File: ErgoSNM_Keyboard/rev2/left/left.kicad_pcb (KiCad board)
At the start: 2 copper layers, 115.6 x 106.7 mm, 111 parts, among them J1 USB_C_Receptacle_USB2.0, J2 USB_C_Receptacle_USB2.0, J3 PJ-393_TRRS_8P, J4 Conn_01x08, SW1 BOOT, SW2 RESET, U1 RT9013-33GB, U2 SRV05-4, U3 W25Q128JVS, U4 RP2040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

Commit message: Update silk and logo
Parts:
- moved kibuzzard-63A148C1 119.2 mm to (73.6, 116.4)
- moved G*** 112.2 mm to (90.3, 114.3)

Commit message: Update logo
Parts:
- moved G*** 20.4 mm to (82.5, 95.4)
- moved kibuzzard-63A148C1 19.2 mm to (74.1, 97.2)

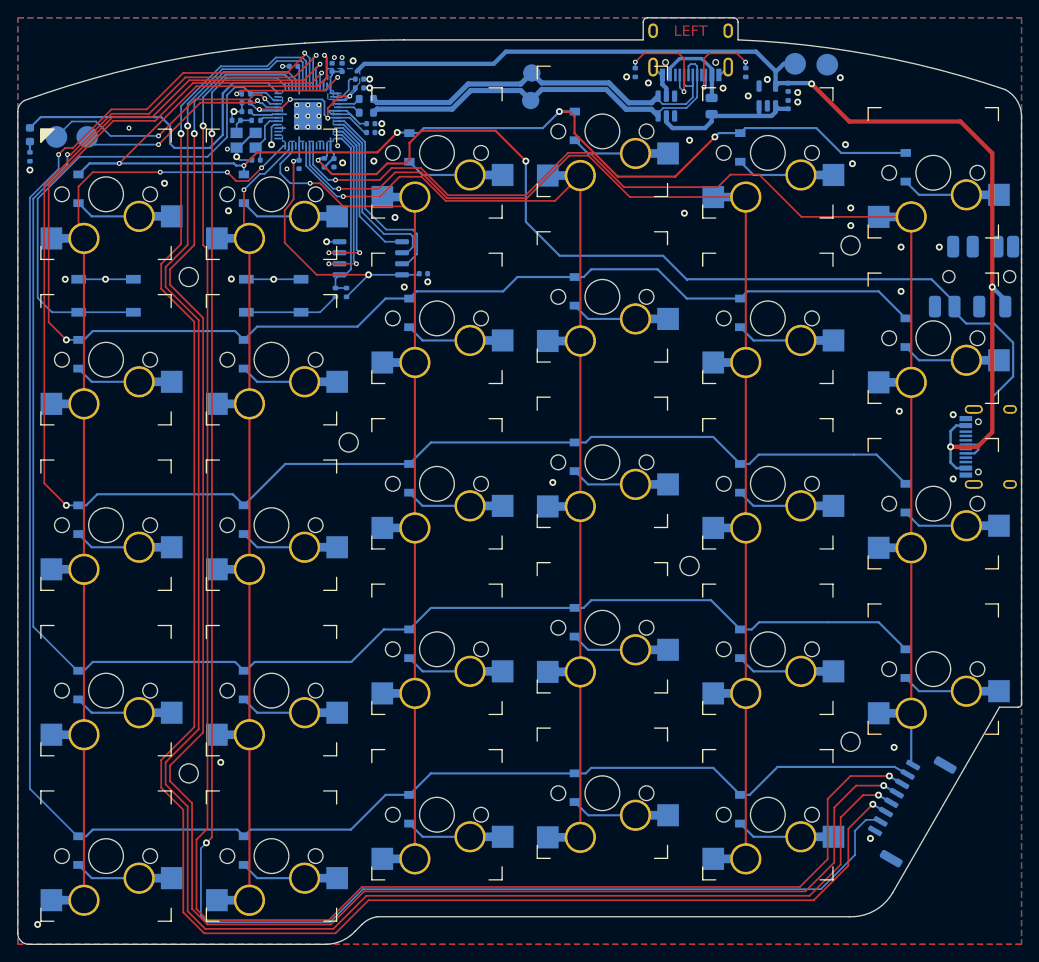
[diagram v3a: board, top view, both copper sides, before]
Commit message: Replace JST GH 1.25 connector with 0.5mm FPC
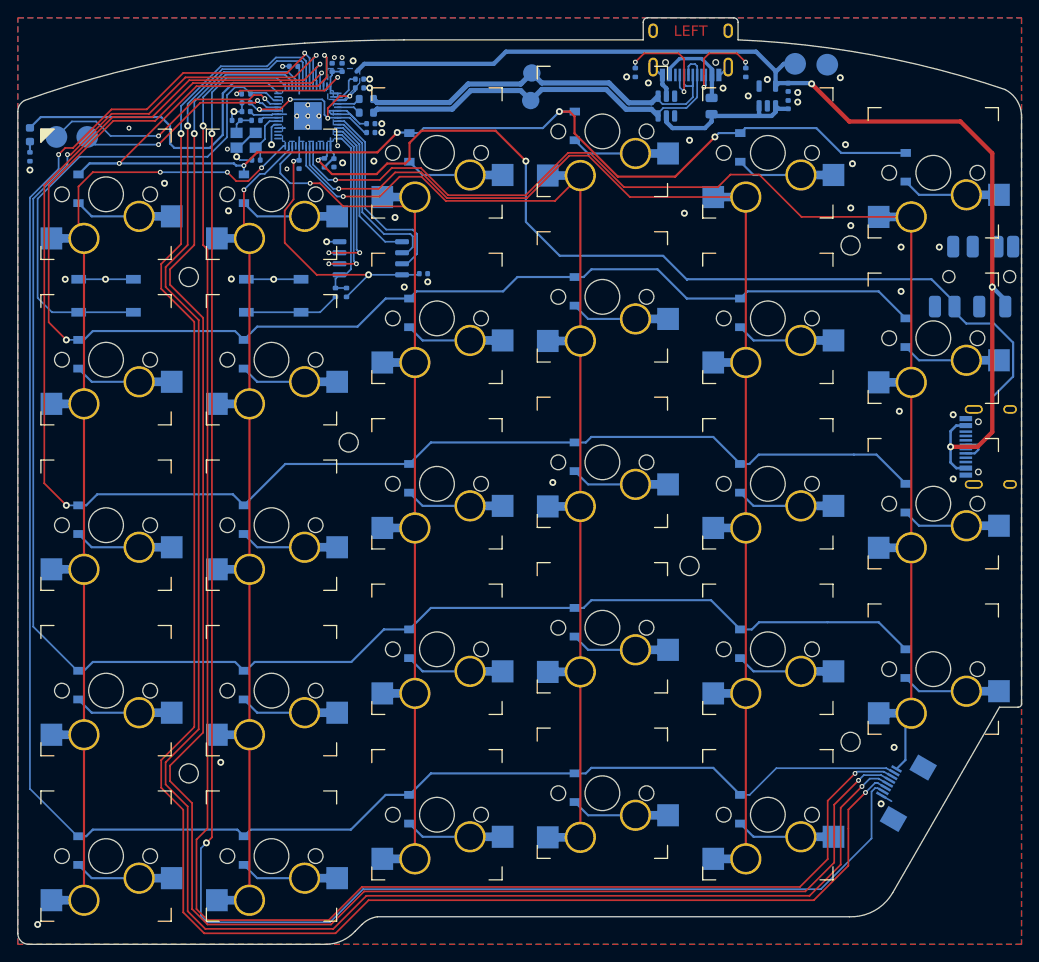
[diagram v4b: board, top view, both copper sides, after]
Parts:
- removed kibuzzard-63A148C1: G***, kibuzzard-63A148C1
- J4: footprint Connector_JST:JST_GH_SM08B-GHS-TB_1x08-1MP_P1.25mm_Horizontal -> ErgoSNM_Keyboard:FPC_8P_0.5mm_AFC01-S08FCA-00
- moved J4 1.31 mm to (163.9, 114.9), turned to 60 degrees
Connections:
- J4 pad 1: COL_5 -> GND
- J4 pad 2: ROW_4 -> Encoder_B
- J4 pad 3: ROW_5 -> Encoder_A
- J4 pad 4: COL_7 -> COL_6
- J4 pad 5: COL_6 -> COL_7
- J4 pad 6: Encoder_A -> ROW_5
- J4 pad 7: Encoder_B -> ROW_4
- J4 pad 8: GND -> COL_5
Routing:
- net Encoder_B: track 190.0 -> 193.4 mm
- net Encoder_A: track 208.6 -> 210.7 mm
- net ROW_4: track 221.8 -> 220.1 mm
- net GND: track 30.9 -> 32.2 mm, vias 62 -> 58
- net ROW_5: track 199.4 -> 198.2 mm
- net COL_5: track 143.1 -> 144.2 mm
- net COL_6: track 208.1 -> 209.0 mm
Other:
- board text added: "Rev ${REVISION}"
